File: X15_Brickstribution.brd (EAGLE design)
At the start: 152.4 x 76.2 mm, 87 parts, among them J1 IPL1-104-01-X-S-K, Q1 310mA/60V/1.6Ω, U5 IC_L4970A, U6 DIODE_STPS1545CT, U7 IC_L4970A, U8 DIODE_STPS1545CT

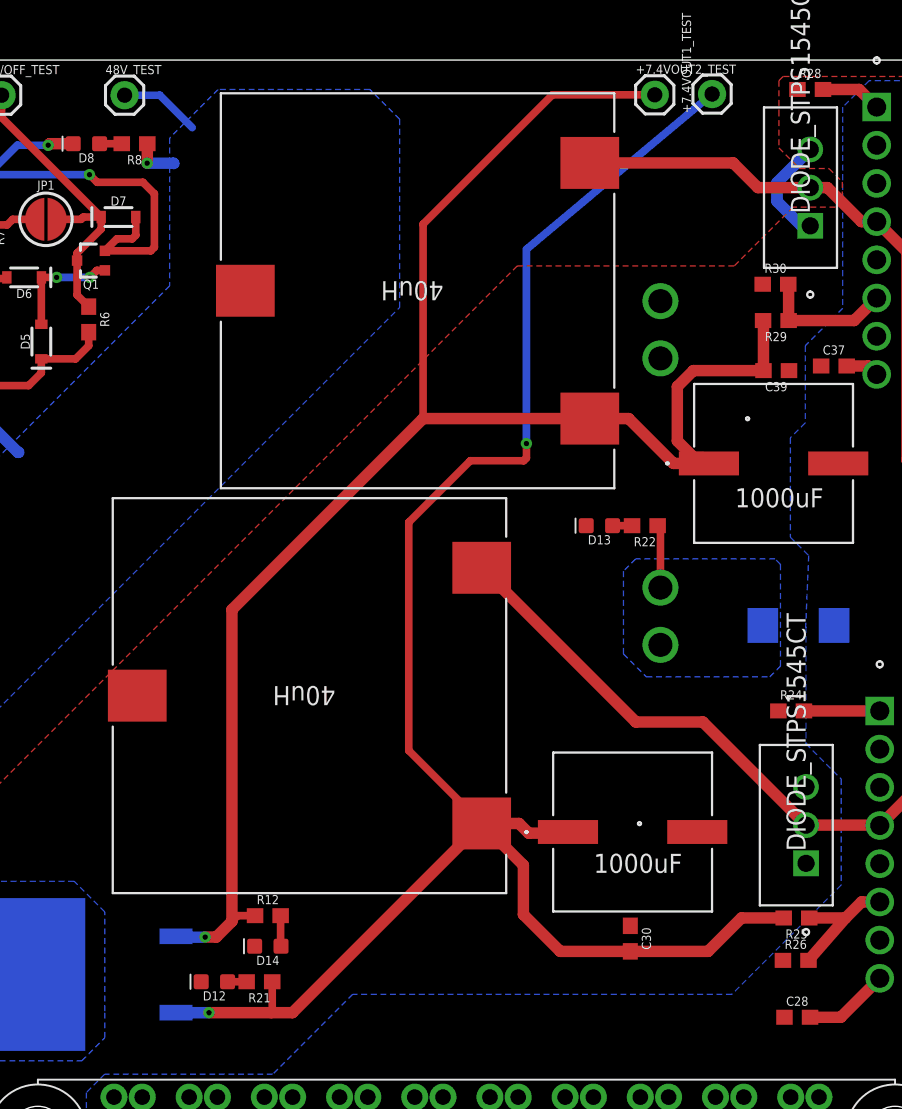
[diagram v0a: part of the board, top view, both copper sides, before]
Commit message: Changed inductor out and reconfigured traces.
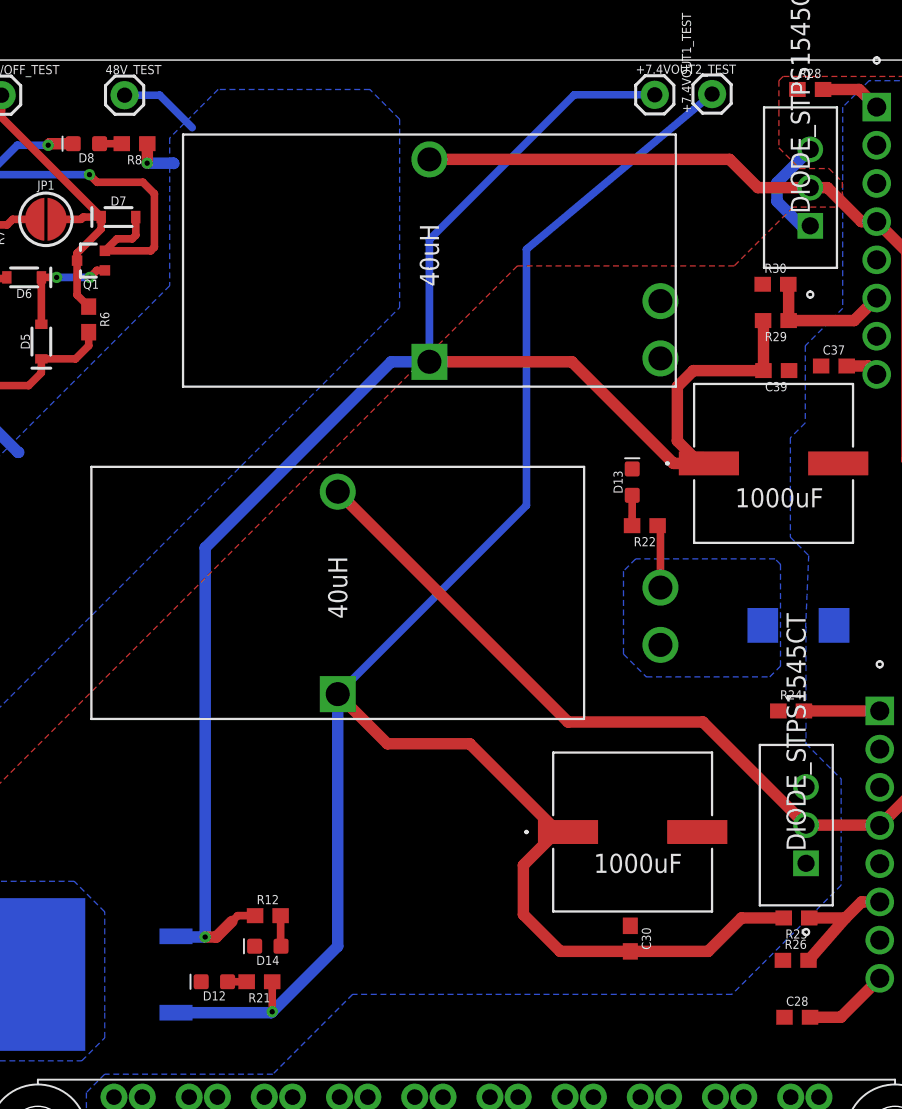
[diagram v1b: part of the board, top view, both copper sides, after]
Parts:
- removed U$5, U$6: 40uH, X15_Brickstribution:TRANS_PG1096_26X26_PUL-M
- added L1, L2: 40uH, X15_Brickstribution:IND_23XX-V_53_53
- moved D13 3.63 mm to (87.9, 48.1), turned to 90 degrees
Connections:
- net OUT1: now also L1.2; no longer U$5.2
- net OUT2: now also L2.2; no longer U$6.2
- net VOUT1: now also L1.1; no longer U$5.1
- net VOUT2: now also L2.1; no longer U$6.1
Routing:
- net OUT1: track 59.4 -> 71.1 mm
- net OUT2: track 62.5 -> 73.3 mm
- net VOUT1: track 121.7 -> 128.0 mm, vias 2 -> 1
- net VOUT2: track 112.6 -> 116.1 mm
- net N$13: track 1.30 -> 2.02 mm

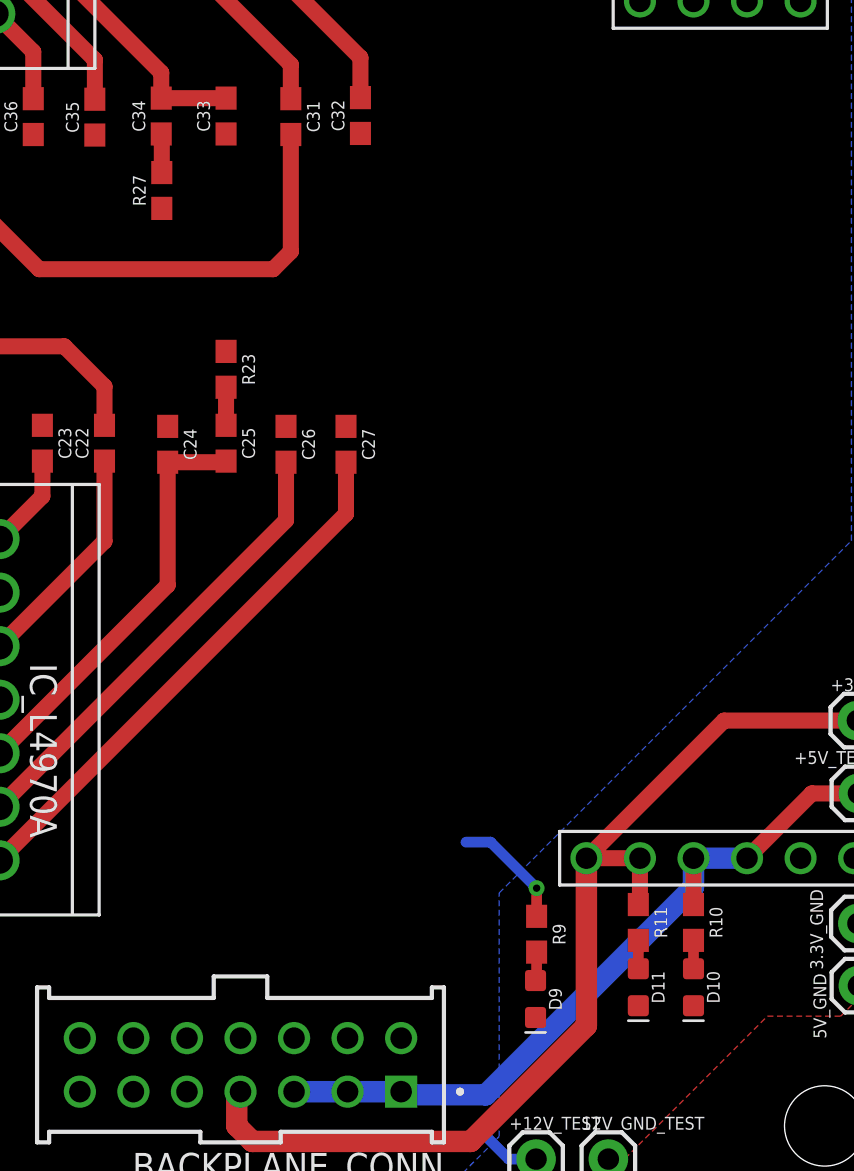
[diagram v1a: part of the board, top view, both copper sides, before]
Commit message: Moved placement of resistors.
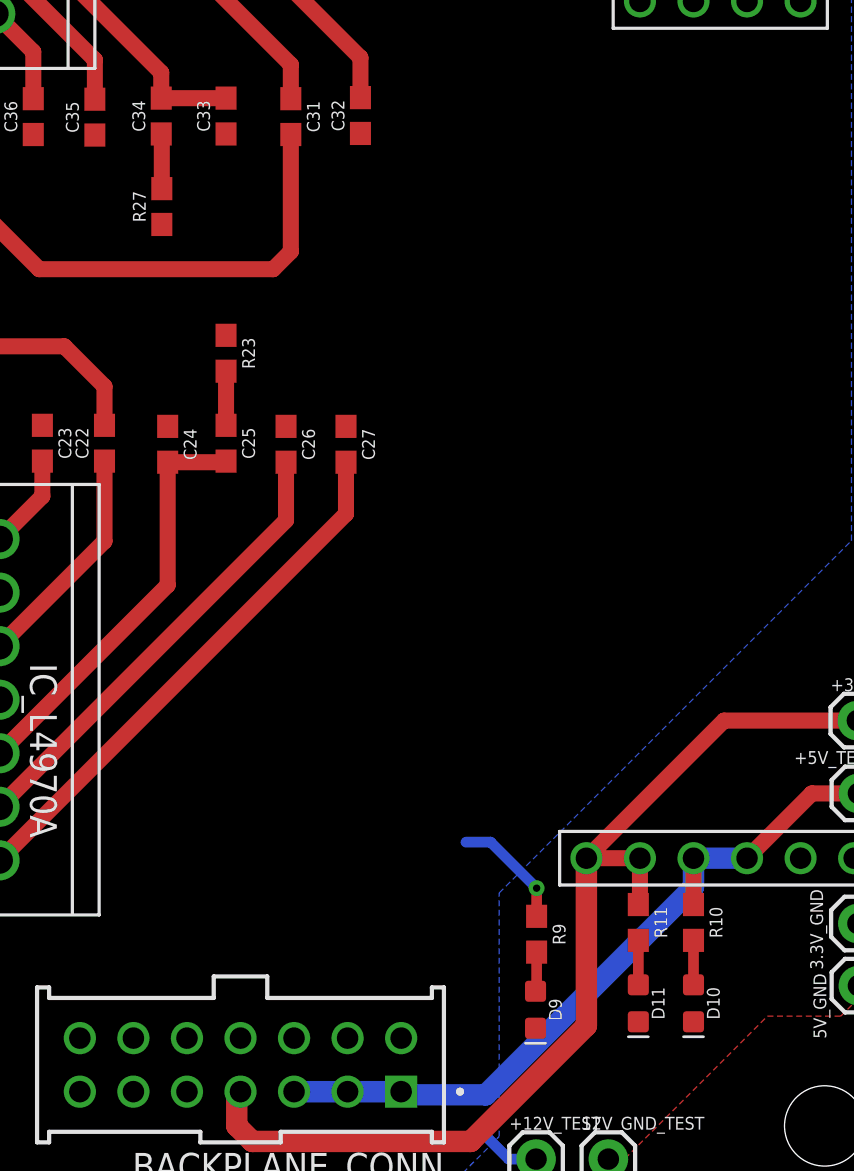
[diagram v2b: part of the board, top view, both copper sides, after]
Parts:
- moved D10 0.76 mm to (142.4, 9.63)
- moved D11 0.76 mm to (139.8, 9.63)
- moved R23 0.76 mm to (120.2, 40.5)
- moved R27 0.76 mm to (117.1, 47.4)
- moved D9 0.51 mm to (134.9, 9.32)
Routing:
- net N$14: track 1.81 -> 2.57 mm
- net N$15: track 1.84 -> 2.60 mm
- net N$9: track 1.35 -> 2.11 mm
- net N$10: track 1.35 -> 2.11 mm
- net N$8: track 1.37 -> 1.88 mm
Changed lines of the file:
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@@
 <attribute name="VALUE" x="51.6128" y="71.2724" size="0.6096" layer="27" font="vector" ratio="20" rot="R180" align="top-center"/>
 </element>
-<element name="D9" library="SparkFun-LED" library_urn="urn:adsk.eagle:library:529" package="LED-0603" package3d_urn="urn:adsk.eagle:package:39354/1" value="GREEN" x="134.874" y="9.8298" smashed="yes" rot="R270">
-<attribute name="NAME" x="135.509" y="9.8298" size="0.6096" layer="25" font="vector" ratio="20" rot="R270" align="bottom-center"/>
-<attribute name="PROD_ID" value="DIO-00821" x="134.874" y="9.8298" size="1.778" layer="27" rot="R270" display="off"/>
-<attribute name="VALUE" x="134.239" y="9.8298" size="0.6096" layer="27" font="vector" ratio="20" rot="R270" align="top-center"/>
-</element>
-<element name="D10" library="SparkFun-LED" library_urn="urn:adsk.eagle:library:529" package="LED-0603" package3d_urn="urn:adsk.eagle:package:39354/1" value="BLUE" x="142.367" y="10.3886" smashed="yes" rot="R270">
-<attribute name="NAME" x="143.002" y="10.3886" size="0.6096" layer="25" font="vector" ratio="20" rot="R270" align="bottom-center"/>
-<attribute name="PROD_ID" value="DIO-08575" x="142.367" y="10.3886" size="1.778" layer="27" rot="R270" display="off"/>
-<attribute name="VALUE" x="141.732" y="10.3886" size="0.6096" layer="27" font="vector" ratio="20" rot="R270" align="top-center"/>
-</element>
-<element name="D11" library="SparkFun-LED" library_urn="urn:adsk.eagle:library:529" package="LED-0603" package3d_urn="urn:adsk.eagle:package:39354/1" value="WHITE" x="139.7508" y="10.3886" smashed="yes" rot="R270">
-<attribute name="NAME" x="140.3858" y="10.3886" size="0.6096" layer="25" font="vector" ratio="20" rot="R270" align="bottom-center"/>
-<attribute name="PROD_ID" value="DIO-09004" x="139.7508" y="10.3886" size="1.778" layer="27" rot="R270" display="off"/>
-<attribute name="VALUE" x="139.1158" y="10.3886" size="0.6096" layer="27" font="vector" ratio="20" rot="R270" align="top-center"/>
+<element name="D9" library="SparkFun-LED" library_urn="urn:adsk.eagle:library:529" package="LED-0603" package3d_urn="urn:adsk.eagle:package:39354/1" value="GREEN" x="134.874" y="9.3218" smashed="yes" rot="R270">
+<attribute name="NAME" x="135.509" y="9.3218" size="0.6096" layer="25" font="vector" ratio="20" rot="R270" align="bottom-center"/>
+<attribute name="PROD_ID" value="DIO-00821" x="134.874" y="9.3218" size="1.778" layer="27" rot="R270" display="off"/>
+<attribute name="VALUE" x="134.239" y="9.3218" size="0.6096" layer="27" font="vector" ratio="20" rot="R270" align="top-center"/>
+</element>
+<element name="D10" library="SparkFun-LED" library_urn="urn:adsk.eagle:library:529" package="LED-0603" package3d_urn="urn:adsk.eagle:package:39354/1" value="BLUE" x="142.367" y="9.6266" smashed="yes" rot="R270">
+<attribute name="NAME" x="143.002" y="9.6266" size="0.6096" layer="25" font="vector" ratio="20" rot="R270" align="bottom-center"/>
+<attribute name="PROD_ID" value="DIO-08575" x="142.367" y="9.6266" size="1.778" layer="27" rot="R270" display="off"/>
+<attribute name="VALUE" x="141.732" y="9.6266" size="0.6096" layer="27" font="vector" ratio="20" rot="R270" align="top-center"/>
+</element>
+<element name="D11" library="SparkFun-LED" library_urn="urn:adsk.eagle:library:529" package="LED-0603" package3d_urn="urn:adsk.eagle:package:39354/1" value="WHITE" x="139.7508" y="9.6266" smashed="yes" rot="R270">
+<attribute name="NAME" x="140.3858" y="9.6266" size="0.6096" layer="25" font="vector" ratio="20" rot="R270" align="bottom-center"/>
+<attribute name="PROD_ID" value="DIO-09004" x="139.7508" y="9.6266" size="1.778" layer="27" rot="R270" display="off"/>
+<attribute name="VALUE" x="139.1158" y="9.6266" size="0.6096" layer="27" font="vector" ratio="20" rot="R270" align="top-center"/>
 </element>
 <element name="+7.4VOUT1_TEST" library="SparkFun-Connectors" library_urn="urn:adsk.eagle:library:513" package="1X01" package3d_urn="urn:adsk.eagle:package:38028/1" value="" x="93.218" y="73.9394" smashed="yes" rot="R90">
@@
 <attribute name="VALUE" x="119.4308" y="36.195" size="0.6096" layer="27" font="vector" ratio="20" rot="R270" align="top-center"/>
 </element>
-<element name="R23" library="SparkFun-Resistors" library_urn="urn:adsk.eagle:library:532" package="0603" package3d_urn="urn:adsk.eagle:package:39650/1" value="15k" x="120.1928" y="39.7002" smashed="yes" rot="R270">
-<attribute name="NAME" x="120.9548" y="39.7002" size="0.6096" layer="25" font="vector" ratio="20" rot="R270" align="bottom-center"/>
-<attribute name="PROD_ID" value="RES-07854" x="195.1228" y="105.7402" size="1.778" layer="27" rot="R270" display="off"/>
-<attribute name="VALUE" x="119.4308" y="39.7002" size="0.6096" layer="27" font="vector" ratio="20" rot="R270" align="top-center"/>
+<element name="R23" library="SparkFun-Resistors" library_urn="urn:adsk.eagle:library:532" package="0603" package3d_urn="urn:adsk.eagle:package:39650/1" value="15k" x="120.1928" y="40.4622" smashed="yes" rot="R270">
+<attribute name="NAME" x="120.9548" y="40.4622" size="0.6096" layer="25" font="vector" ratio="20" rot="R270" align="bottom-center"/>
+<attribute name="PROD_ID" value="RES-07854" x="195.1228" y="106.5022" size="1.778" layer="27" rot="R270" display="off"/>
+<attribute name="VALUE" x="119.4308" y="40.4622" size="0.6096" layer="27" font="vector" ratio="20" rot="R270" align="top-center"/>
 </element>
 <element name="R24" library="SparkFun-Resistors" library_urn="urn:adsk.eagle:library:532" package="0603" package3d_urn="urn:adsk.eagle:package:39650/1" value="16k" x="98.4758" y="32.9184" smashed="yes">
@@
 <attribute name="VALUE" x="117.8814" y="51.7144" size="0.6096" layer="27" font="vector" ratio="20" rot="R90" align="top-center"/>
 </element>
-<element name="R27" library="SparkFun-Resistors" library_urn="urn:adsk.eagle:library:532" package="0603" package3d_urn="urn:adsk.eagle:package:39650/1" value="15k" x="117.1448" y="48.1838" smashed="yes" rot="R90">
-<attribute name="NAME" x="116.3828" y="48.1838" size="0.6096" layer="25" font="vector" ratio="20" rot="R90" align="bottom-center"/>
-<attribute name="PROD_ID" value="RES-07854" x="159.0548" y="-78.8162" size="1.778" layer="27" rot="R90" display="off"/>
-<attribute name="VALUE" x="117.9068" y="48.1838" size="0.6096" layer="27" font="vector" ratio="20" rot="R90" align="top-center"/>
+<element name="R27" library="SparkFun-Resistors" library_urn="urn:adsk.eagle:library:532" package="0603" package3d_urn="urn:adsk.eagle:package:39650/1" value="15k" x="117.1448" y="47.4218" smashed="yes" rot="R90">
+<attribute name="NAME" x="116.3828" y="47.4218" size="0.6096" layer="25" font="vector" ratio="20" rot="R90" align="bottom-center"/>
+<attribute name="PROD_ID" value="RES-07854" x="159.0548" y="-79.5782" size="1.778" layer="27" rot="R90" display="off"/>
+<attribute name="VALUE" x="117.9068" y="47.4218" size="0.6096" layer="27" font="vector" ratio="20" rot="R90" align="top-center"/>
 </element>
 <element name="R28" library="SparkFun-Resistors" library_urn="urn:adsk.eagle:library:532" package="0603" package3d_urn="urn:adsk.eagle:package:39650/1" value="16k" x="99.7458" y="74.2442" smashed="yes">
@@
 <contactref element="R9" pad="2"/>
 <contactref element="D9" pad="A"/>
-<wire x1="134.9248" y1="12.0532" x2="134.9248" y2="10.7576" width="0.508" layer="1"/>
-<wire x1="134.9248" y1="10.7576" x2="134.874" y2="10.7068" width="0.508" layer="1"/>
+<wire x1="134.9248" y1="12.0532" x2="134.9248" y2="10.2496" width="0.508" layer="1"/>
+<wire x1="134.9248" y1="10.2496" x2="134.874" y2="10.1988" width="0.508" layer="1"/>
 </signal>
 <signal name="N$9">
 <contactref element="R10" pad="2"/>
 <contactref element="D10" pad="A"/>
-<wire x1="142.367" y1="12.612" x2="142.367" y2="11.2656" width="0.508" layer="1"/>
+<wire x1="142.367" y1="12.612" x2="142.367" y2="10.5036" width="0.508" layer="1"/>
 </signal>
 <signal name="N$10">
 <contactref element="R11" pad="2"/>
 <contactref element="D11" pad="A"/>
-<wire x1="139.7508" y1="12.612" x2="139.7508" y2="11.2656" width="0.508" layer="1"/>
+<wire x1="139.7508" y1="12.612" x2="139.7508" y2="10.5036" width="0.508" layer="1"/>
 </signal>
 <signal name="BOOT2">
@@
 <contactref element="C25" pad="1"/>
 <contactref element="R23" pad="2"/>
-<wire x1="120.1928" y1="37.045" x2="120.1928" y2="38.8502" width="0.762" layer="1"/>
+<wire x1="120.1928" y1="37.045" x2="120.1928" y2="39.6122" width="0.762" layer="1"/>
 </signal>
 <signal name="N$15">
@@
 <contactref element="R27" pad="2"/>
 <wire x1="117.1194" y1="50.8644" x2="117.1448" y2="50.839" width="0.762" layer="1"/>
-<wire x1="117.1448" y1="50.839" x2="117.1448" y2="49.0338" width="0.762" layer="1"/>
+<wire x1="117.1448" y1="50.839" x2="117.1448" y2="48.2718" width="0.762" layer="1"/>
 </signal>
 <signal name="N$11">
